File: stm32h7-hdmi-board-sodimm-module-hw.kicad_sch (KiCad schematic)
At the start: 0 parts

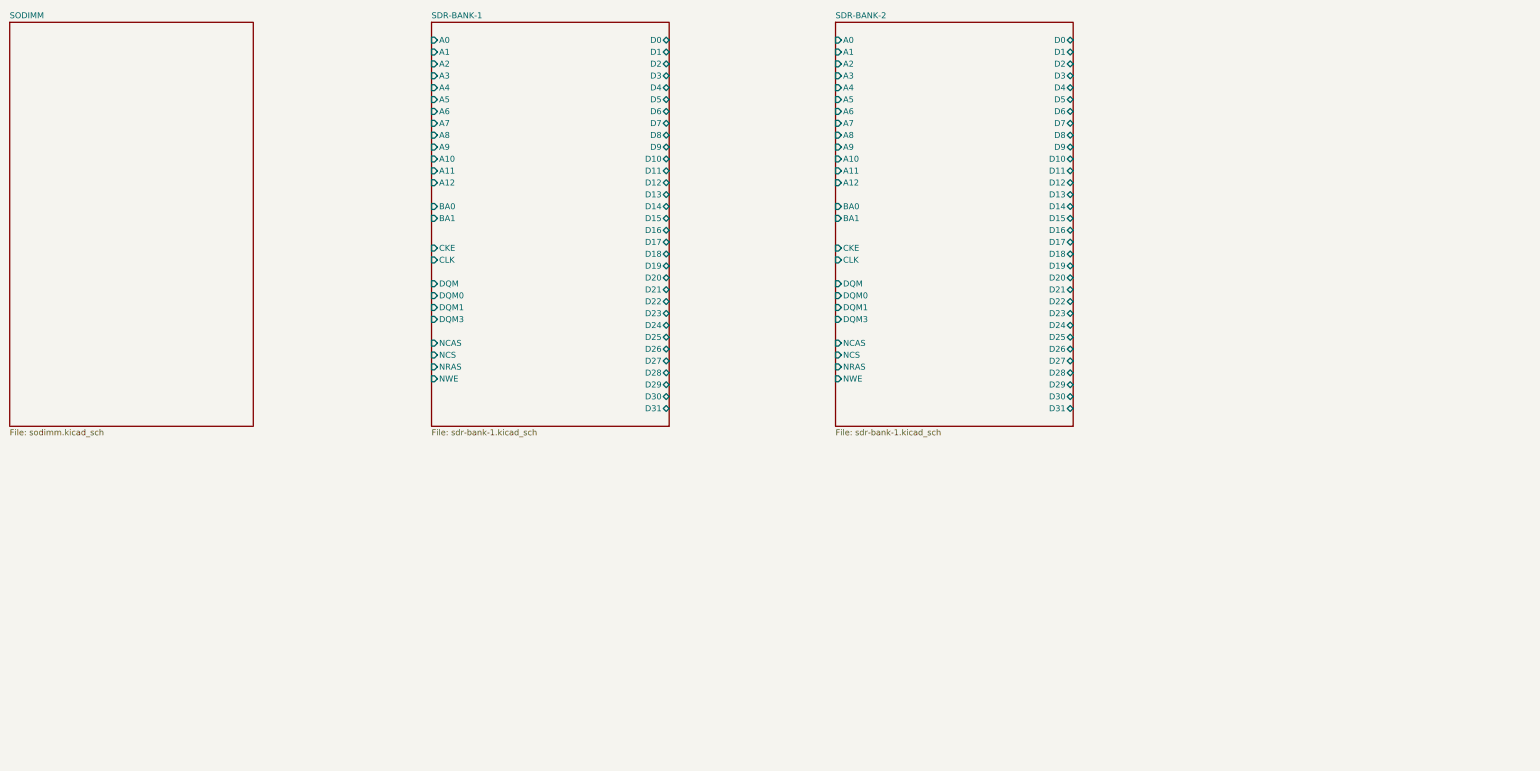
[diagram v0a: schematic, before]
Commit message: [#100470] Connect SODIMM to SDRAM banks
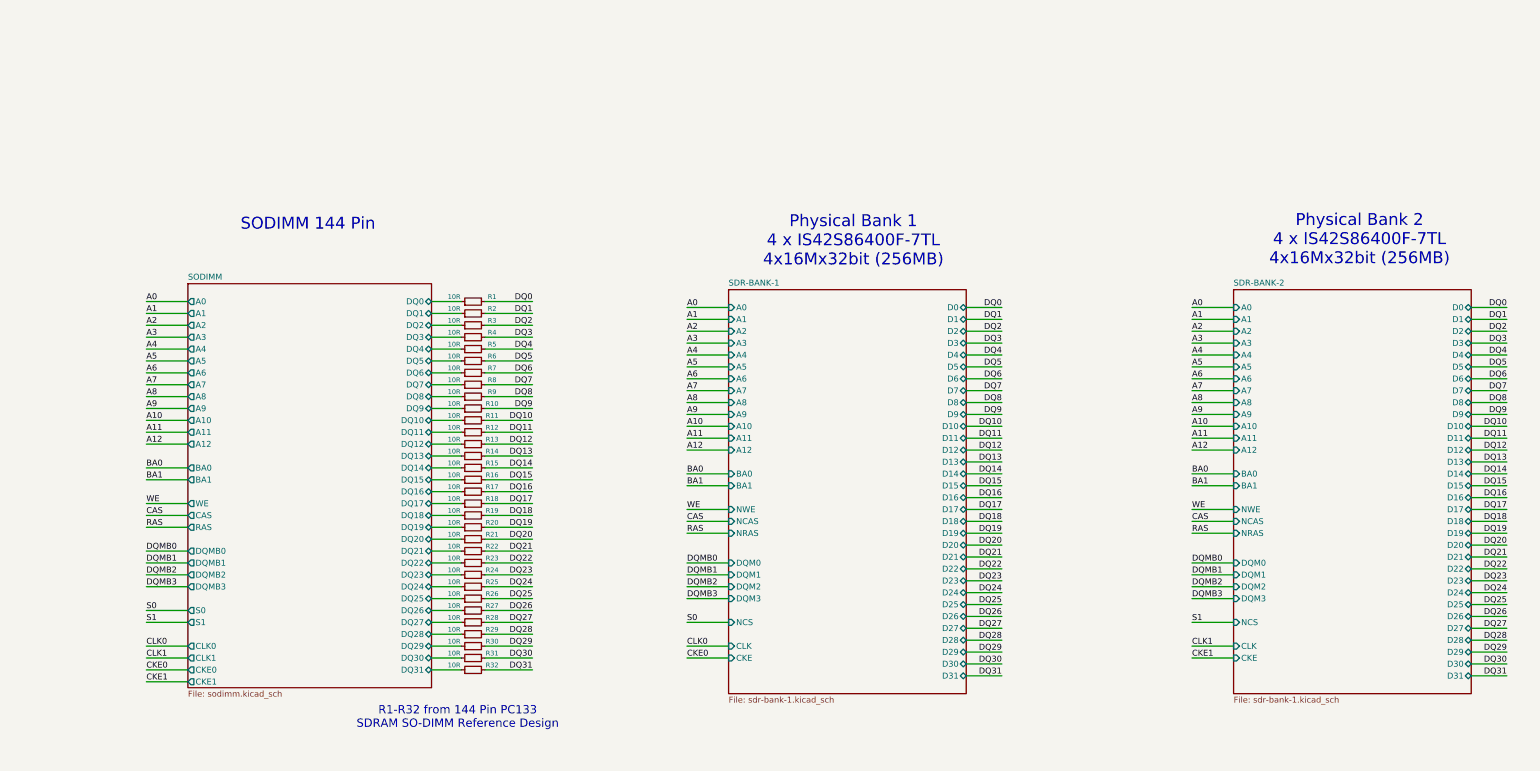
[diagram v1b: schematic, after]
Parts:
- added R1, R10, R11, R12, R13, R14, R15, R16, R17, R18, R19, R2, R20, R21, R22, R23, R24, R25, R26, R27, R28, R29, R3, R30, R31, R32, R4, R5, R6, R7, R8, R9: 10R, symbol Device:R_Small
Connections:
- new net DQ0: R1.2
- new net DQ1: R2.2
- new net DQ10: R11.2
- new net DQ11: R12.2
- new net DQ12: R13.2
- new net DQ13: R14.2
- new net DQ14: R15.2
- new net DQ15: R16.2
- new net DQ16: R17.2
- new net DQ17: R18.2
- new net DQ18: R19.2
- new net DQ19: R20.2
- new net DQ2: R3.2
- new net DQ20: R21.2
- new net DQ21: R22.2
- new net DQ22: R23.2
- new net DQ23: R24.2
- new net DQ24: R25.2
- new net DQ25: R26.2
- new net DQ26: R27.2
- new net DQ27: R28.2
- new net DQ28: R29.2
- new net DQ29: R30.2
- new net DQ3: R4.2
- new net DQ30: R31.2
- new net DQ31: R32.2
- new net DQ4: R5.2
- new net DQ5: R6.2
- new net DQ6: R7.2
- new net DQ7: R8.2
- new net DQ8: R9.2
- new net DQ9: R10.2
- new net SODIMM/DQ0: R1.1
- new net SODIMM/DQ1: R2.1
- new net SODIMM/DQ10: R11.1
- new net SODIMM/DQ11: R12.1
- new net SODIMM/DQ12: R13.1
- new net SODIMM/DQ13: R14.1
- new net SODIMM/DQ14: R15.1
- new net SODIMM/DQ15: R16.1
- new net SODIMM/DQ16: R17.1
- new net SODIMM/DQ17: R18.1
- new net SODIMM/DQ18: R19.1
- new net SODIMM/DQ19: R20.1
- new net SODIMM/DQ2: R3.1
- new net SODIMM/DQ20: R21.1
- new net SODIMM/DQ21: R22.1
- new net SODIMM/DQ22: R23.1
- new net SODIMM/DQ23: R24.1
- new net SODIMM/DQ24: R25.1
- new net SODIMM/DQ25: R26.1
- new net SODIMM/DQ26: R27.1
- new net SODIMM/DQ27: R28.1
- new net SODIMM/DQ28: R29.1
- new net SODIMM/DQ29: R30.1
- new net SODIMM/DQ3: R4.1
- new net SODIMM/DQ30: R31.1
- new net SODIMM/DQ31: R32.1
- new net SODIMM/DQ4: R5.1
- new net SODIMM/DQ5: R6.1
- new net SODIMM/DQ6: R7.1
- new net SODIMM/DQ7: R8.1
- new net SODIMM/DQ8: R9.1
- new net SODIMM/DQ9: R10.1
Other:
- sheet SDR-BANK-1 ports: added DQM2; removed DQM
- sheet SDR-BANK-2 ports: added DQM2; removed DQM
- sheet SODIMM ports: added A0, A1, A10, A11, A12, A2, A3, A4, A5, A6, A7, A8, A9, BA0, BA1, CAS, CKE0, CKE1, CLK0, CLK1, DQ0, DQ1, DQ10, DQ11, DQ12, DQ13, DQ14, DQ15, DQ16, DQ17, DQ18, DQ19, DQ2, DQ20, DQ21, DQ22, DQ23, DQ24, DQ25, DQ26, DQ27, DQ28, DQ29, DQ3, DQ30, DQ31, DQ4, DQ5, DQ6, DQ7, DQ8, DQ9, DQMB0, DQMB1, DQMB2, DQMB3, RAS, S0, S1, WE; removed none
- note added: "Physical Bank 1 4 x IS42S86400F-7TL 4x16Mx32bit (256MB)"
- note added: "Physical Bank 2 4 x IS42S86400F-7TL 4x16Mx32bit (256MB)"
- note added: "R1-R32 from 144 Pin PC133 SDRAM SO-DIMM Reference Design"
- note added: "SODIMM 144 Pin"
- company: (none) -> Antmicro Ltd
- title: (none) -> STM32H7 HDMI Board SODIMM

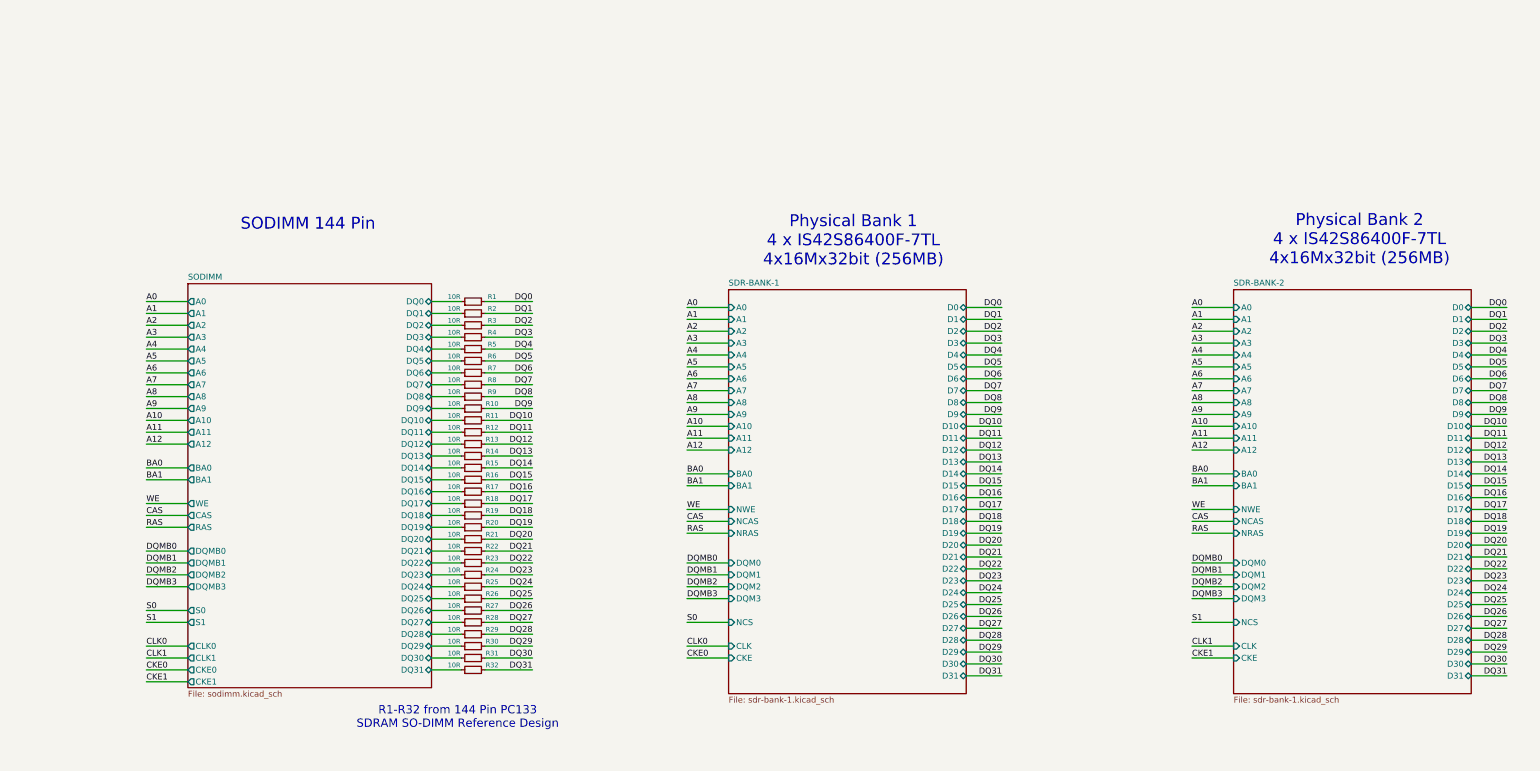
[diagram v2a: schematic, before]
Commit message: [#100470] Switch to R in packs, assign footprints
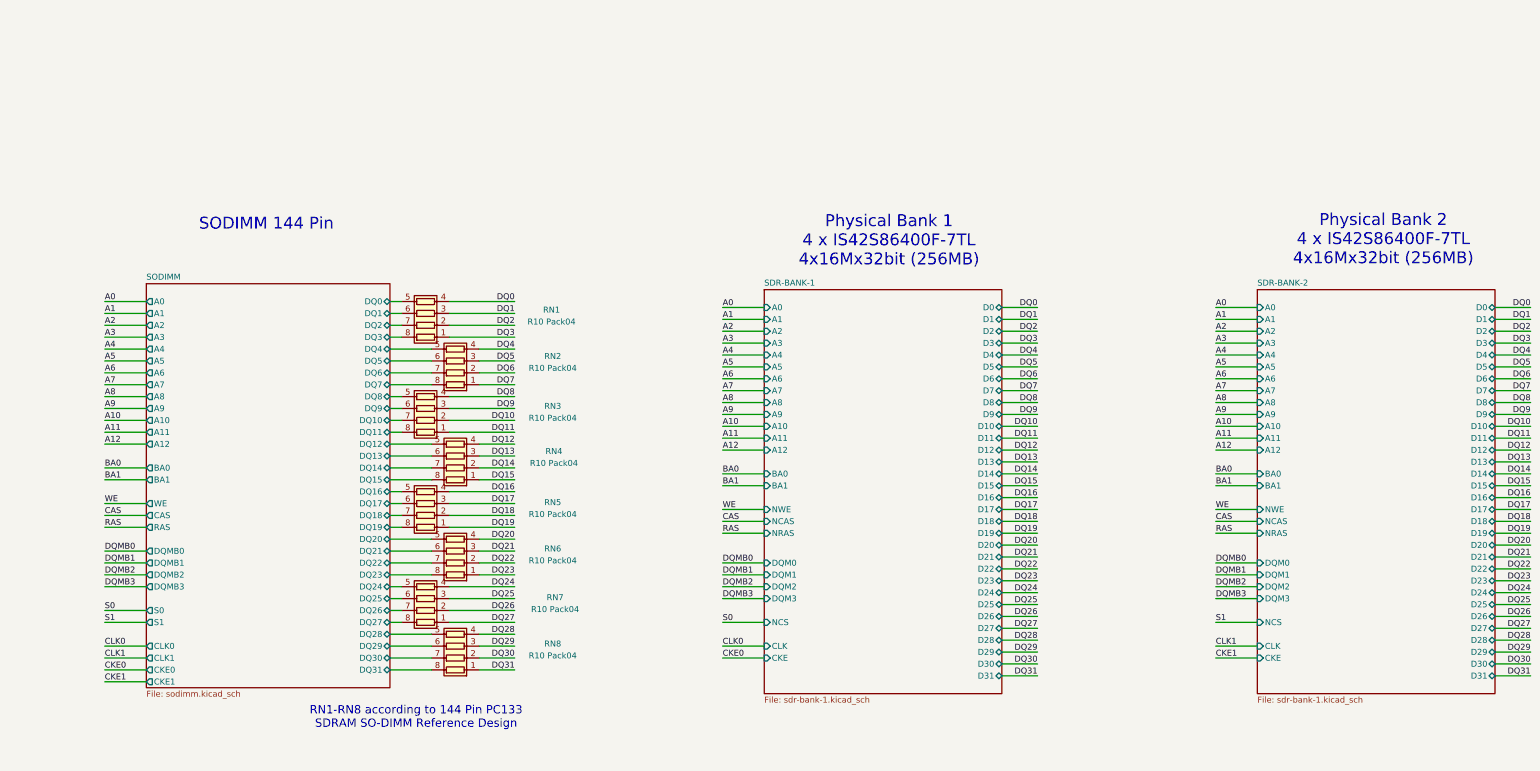
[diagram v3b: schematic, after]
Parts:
- removed R1, R10, R11, R12, R13, R14, R15, R16, R17, R18, R19, R2, R20, R21, R22, R23, R24, R25, R26, R27, R28, R29, R3, R30, R31, R32, R4, R5, R6, R7, R8, R9: 10R, symbol Device:R_Small
- added RN1, RN2, RN3, RN4, RN5, RN6, RN7, RN8: R10 Pack04, Resistor_SMD:R_Array_Convex_4x0603, symbol Device:R_Pack04
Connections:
- net DQ0: now also RN1.4 (R4.1)
- net DQ1: now also RN1.3 (R3.1)
- net DQ10: now also RN3.2 (R2.1)
- net DQ11: now also RN3.1 (R1.1)
- net DQ12: now also RN4.4 (R4.1)
- net DQ13: now also RN4.3 (R3.1)
- net DQ14: now also RN4.2 (R2.1)
- net DQ15: now also RN4.1 (R1.1)
- net DQ16: now also RN5.4 (R4.1)
- net DQ17: now also RN5.3 (R3.1)
- net DQ18: now also RN5.2 (R2.1)
- net DQ19: now also RN5.1 (R1.1)
- net DQ2: now also RN1.2 (R2.1)
- net DQ20: now also RN6.4 (R4.1)
- net DQ21: now also RN6.3 (R3.1)
- net DQ22: now also RN6.2 (R2.1)
- net DQ23: now also RN6.1 (R1.1)
- net DQ24: now also RN7.4 (R4.1)
- net DQ25: now also RN7.3 (R3.1)
- net DQ26: now also RN7.2 (R2.1)
- net DQ27: now also RN7.1 (R1.1)
- net DQ28: now also RN8.4 (R4.1)
- net DQ29: now also RN8.3 (R3.1)
- net DQ3: now also RN1.1 (R1.1)
- net DQ30: now also RN8.2 (R2.1)
- net DQ31: now also RN8.1 (R1.1)
- net DQ4: now also RN2.4 (R4.1)
- net DQ5: now also RN2.3 (R3.1)
- net DQ6: now also RN2.2 (R2.1)
- net DQ7: now also RN2.1 (R1.1)
- net DQ8: now also RN3.4 (R4.1)
- net DQ9: now also RN3.3 (R3.1)
- net SODIMM/DQ0: now also RN1.5 (R4.2)
- net SODIMM/DQ1: now also RN1.6 (R3.2)
- net SODIMM/DQ10: now also RN3.7 (R2.2)
- net SODIMM/DQ11: now also RN3.8 (R1.2)
- net SODIMM/DQ12: now also RN4.5 (R4.2)
- net SODIMM/DQ13: now also RN4.6 (R3.2)
- net SODIMM/DQ14: now also RN4.7 (R2.2)
- net SODIMM/DQ15: now also RN4.8 (R1.2)
- net SODIMM/DQ16: now also RN5.5 (R4.2)
- net SODIMM/DQ17: now also RN5.6 (R3.2)
- net SODIMM/DQ18: now also RN5.7 (R2.2)
- net SODIMM/DQ19: now also RN5.8 (R1.2)
- net SODIMM/DQ2: now also RN1.7 (R2.2)
- net SODIMM/DQ20: now also RN6.5 (R4.2)
- net SODIMM/DQ21: now also RN6.6 (R3.2)
- net SODIMM/DQ22: now also RN6.7 (R2.2)
- net SODIMM/DQ23: now also RN6.8 (R1.2)
- net SODIMM/DQ24: now also RN7.5 (R4.2)
- net SODIMM/DQ25: now also RN7.6 (R3.2)
- net SODIMM/DQ26: now also RN7.7 (R2.2)
- net SODIMM/DQ27: now also RN7.8 (R1.2)
- net SODIMM/DQ28: now also RN8.5 (R4.2)
- net SODIMM/DQ29: now also RN8.6 (R3.2)
- net SODIMM/DQ3: now also RN1.8 (R1.2)
- net SODIMM/DQ30: now also RN8.7 (R2.2)
- net SODIMM/DQ31: now also RN8.8 (R1.2)
- net SODIMM/DQ4: now also RN2.5 (R4.2)
- net SODIMM/DQ5: now also RN2.6 (R3.2)
- net SODIMM/DQ6: now also RN2.7 (R2.2)
- net SODIMM/DQ7: now also RN2.8 (R1.2)
- net SODIMM/DQ8: now also RN3.5 (R4.2)
- net SODIMM/DQ9: now also RN3.6 (R3.2)
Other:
- note added: "RN1-RN8 according to 144 Pin PC133 SDRAM SO-DIMM Reference Design"
- note removed: "R1-R32 from 144 Pin PC133 SDRAM SO-DIMM Reference Design"

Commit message: [#100470] Update schematic
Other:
- sheet SDR-BANK-1 ports: added A[0..12], D[0..31]; removed A0, A1, A10, A11, A12, A2, A3, A4, A5, A6, A7, A8, A9, D0, D1, D10, D11, D12, D13, D14, D15, D16, D17, D18, D19, D2, D20, D21, D22, D23, D24, D25, D26, D27, D28, D29, D3, D30, D31, D4, D5, D6, D7, D8, D9
- sheet SDR-BANK-2 ports: added A[0..12], D[0..31]; removed A0, A1, A10, A11, A12, A2, A3, A4, A5, A6, A7, A8, A9, D0, D1, D10, D11, D12, D13, D14, D15, D16, D17, D18, D19, D2, D20, D21, D22, D23, D24, D25, D26, D27, D28, D29, D3, D30, D31, D4, D5, D6, D7, D8, D9
- sheet SODIMM ports: added A[0..12]; removed A0, A1, A10, A11, A12, A2, A3, A4, A5, A6, A7, A8, A9
